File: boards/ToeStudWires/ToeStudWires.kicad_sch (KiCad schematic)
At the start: 27 parts

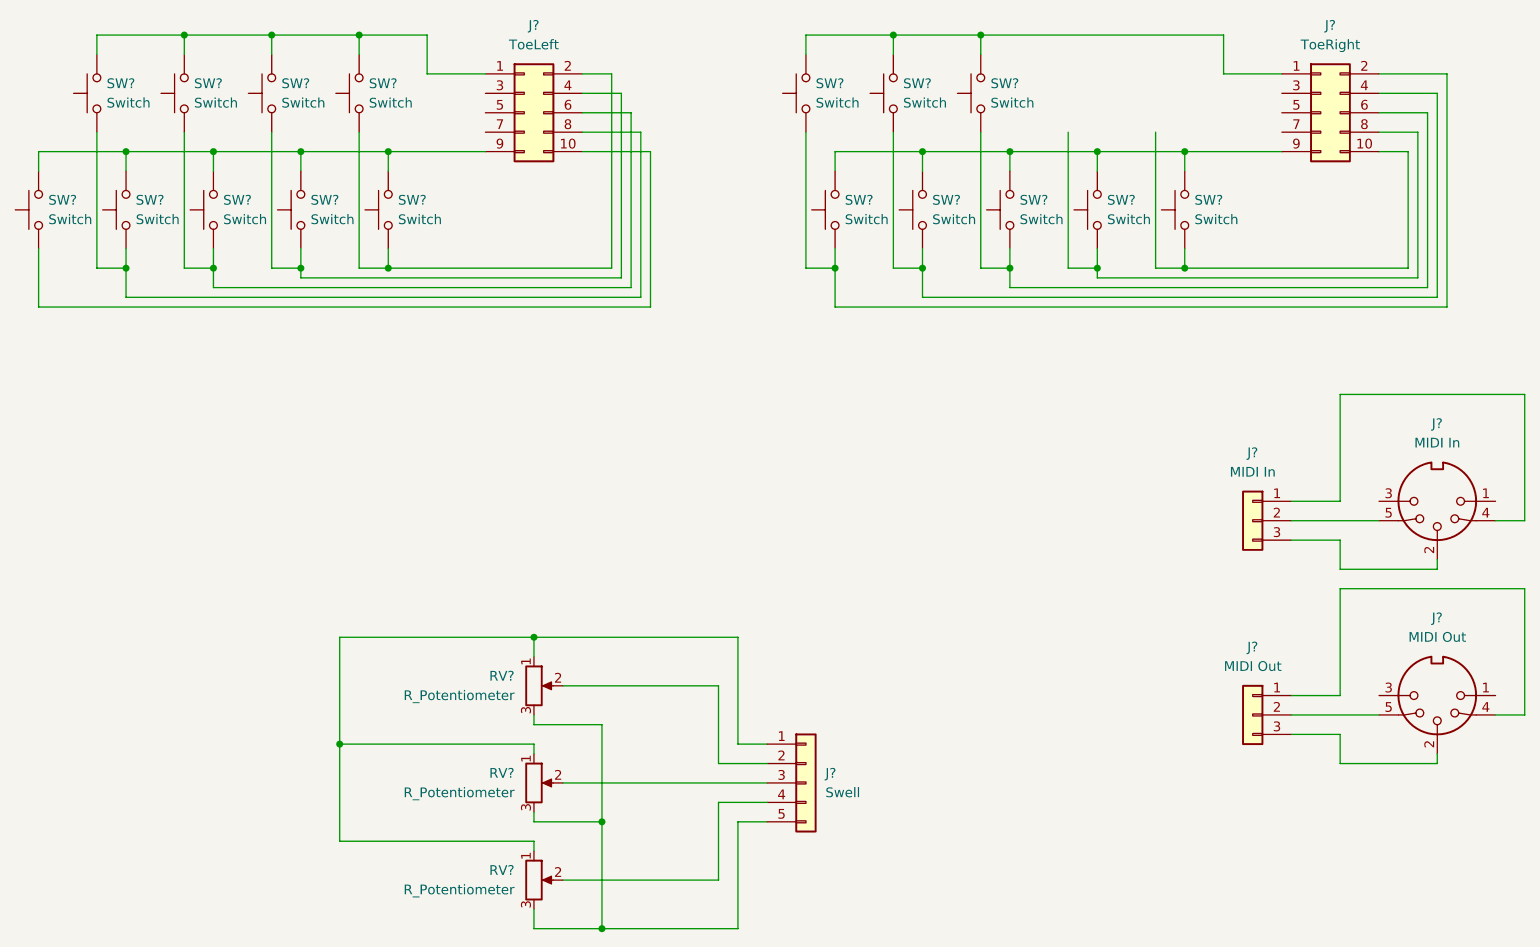
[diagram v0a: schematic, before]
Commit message: Renamed PCBs and updated to KiCAD 7.0
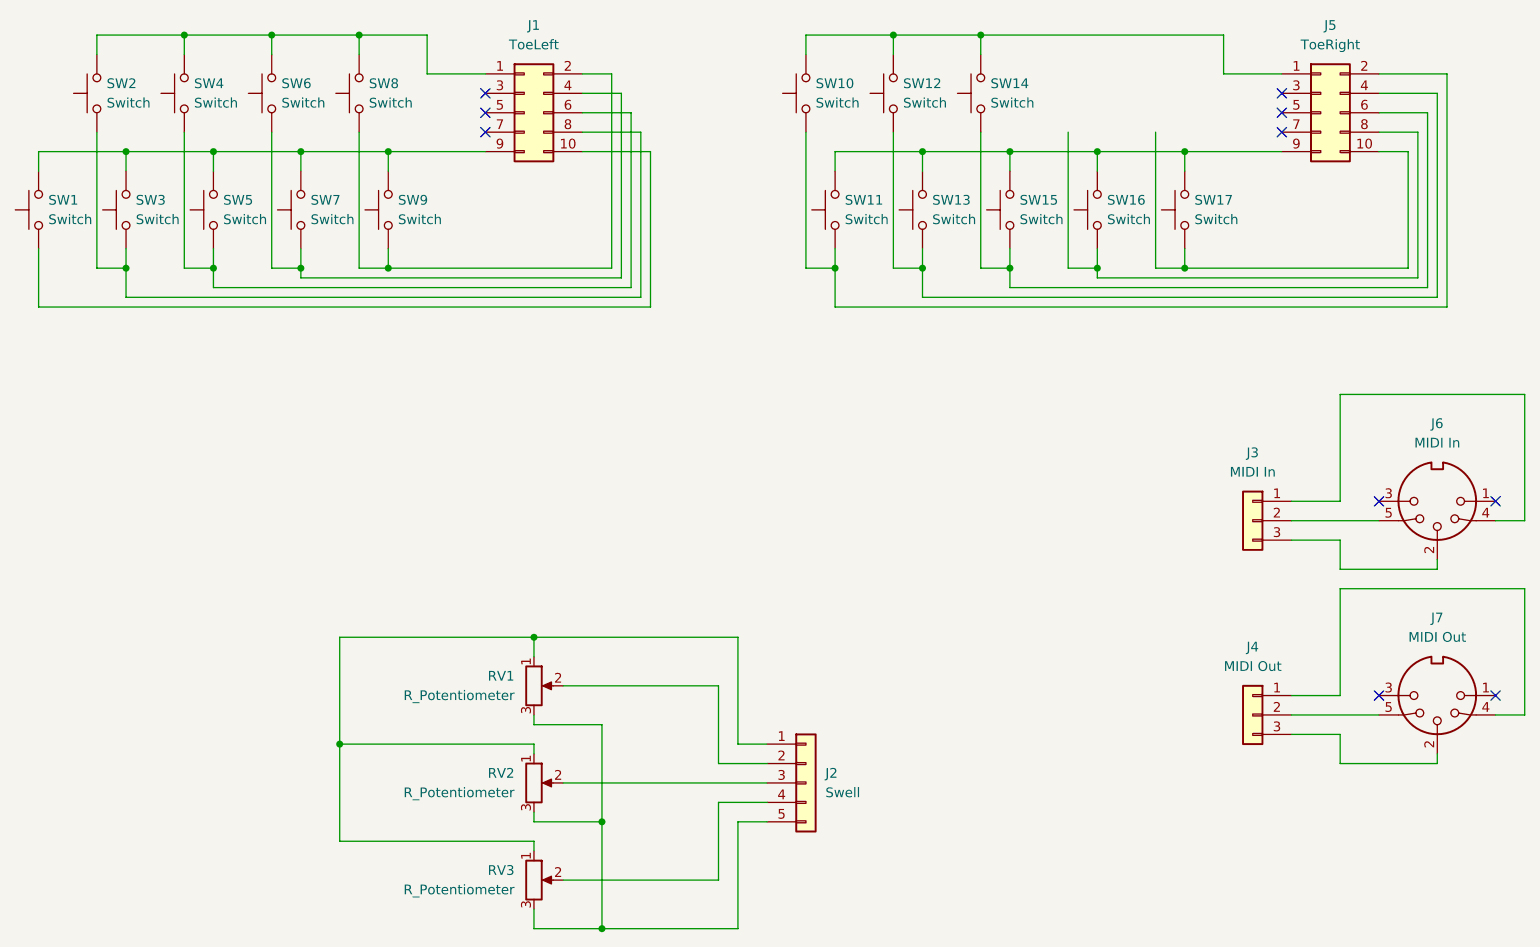
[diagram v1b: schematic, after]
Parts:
- gave numbers to parts that had none: 27
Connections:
- no-connect marks 0 -> 10
